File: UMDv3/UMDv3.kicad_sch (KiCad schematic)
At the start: 61 parts, among them CON101 USB-B1HSB6, CON104 JTAG-2X10-HDR, CON105 101-00405-75, CON106 UMDv3-CONN, CON107 HDR1X3, SW101 PTS645SM43SMTR92_LFS, SW102 PTS645SM43SMTR92_LFS, SW103 PTS645SM43SMTR92_LFS, SW104 PTS645SM43SMTR92_LFS, SW105 PTS645SM43SMTR92_LFS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

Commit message: betterer
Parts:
- removed U104: SSD1106-1.3-OLED-I2C, db-thparts:OLED-1.3-I2C, symbol db-sem:SSD1106-1.3-OLED-I2C
- added MEC105, MEC106: NSP-4-6-01, db-thparts:4-40-SCREW, symbol db-electromech:NSP-4-6-01
- added TP102: TP_2.25x3_ROUNDED, db-smt:TP_2.25x3_RND, symbol db-connectors:TP_2.25x3_ROUNDED
- added U104: SSD1106-0.96-OLED-I2C, db-thparts:OLED-0.96-I2C, symbol db-sem:SSD1106-0.96-OLED-I2C
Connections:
- net +3V3: now also U104.2 (VCC)
- net GND: now also TP102.1, U104.1 (GND)
- net SCL: now also U104.3 (SCL)
- net SDA: now also U104.4 (SDA)
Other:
- moved on the sheet: MEC101, MEC102, MEC103, MEC104, logo101

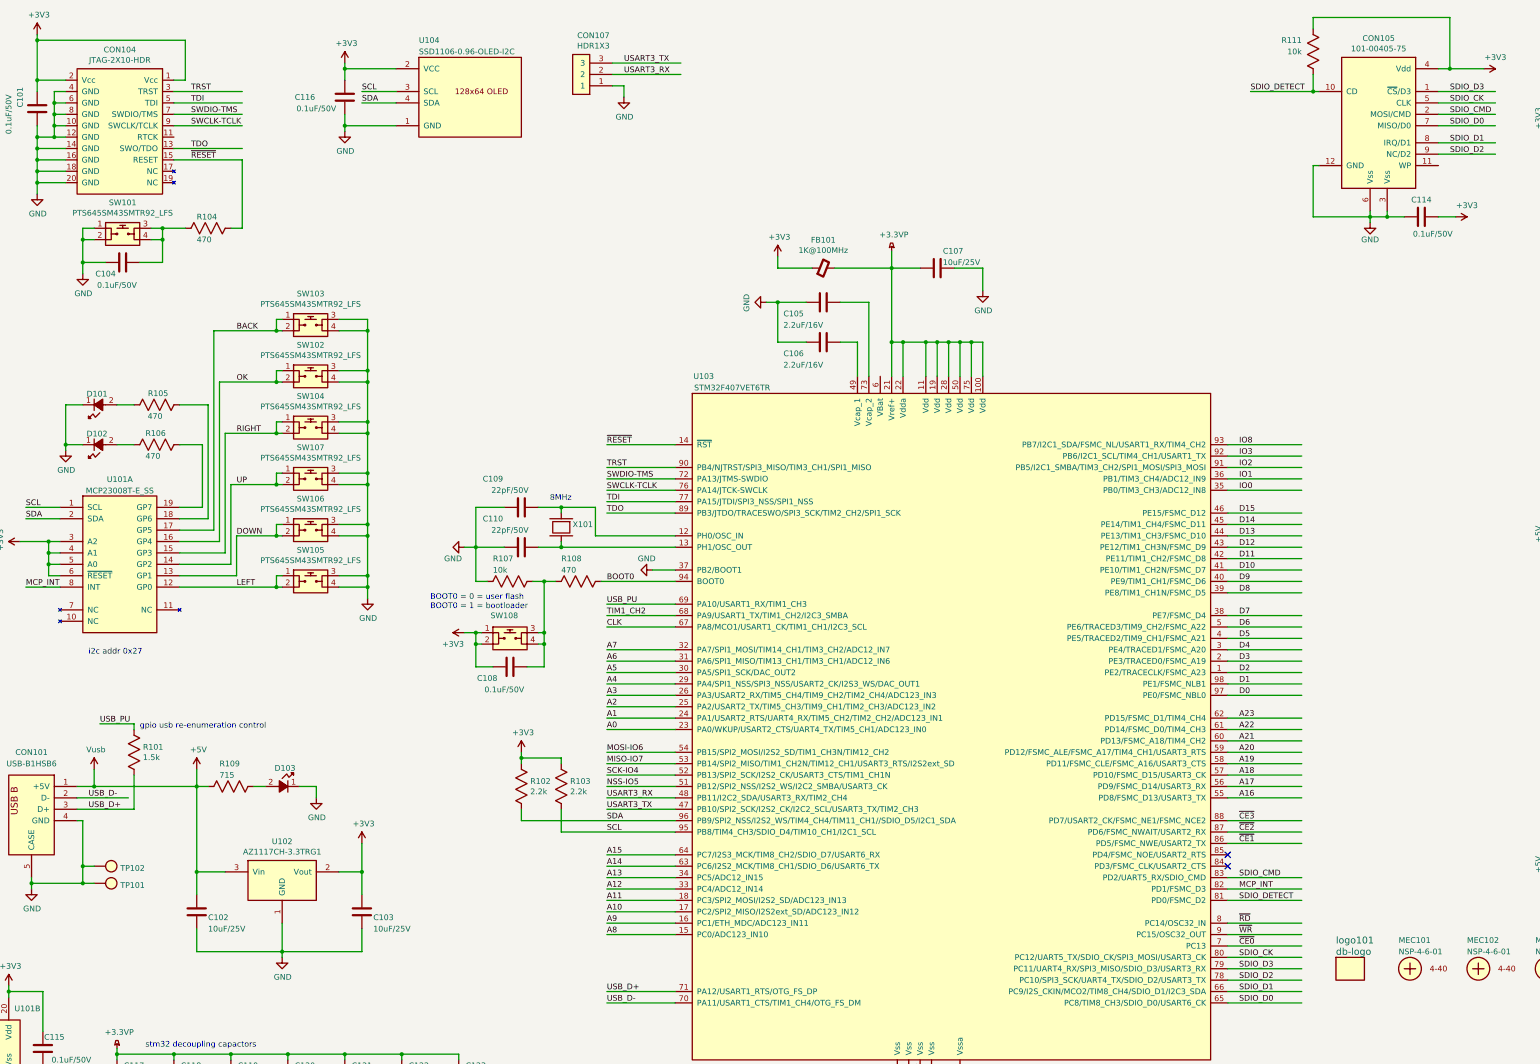
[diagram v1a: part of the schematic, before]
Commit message: more better decoupling capacitance
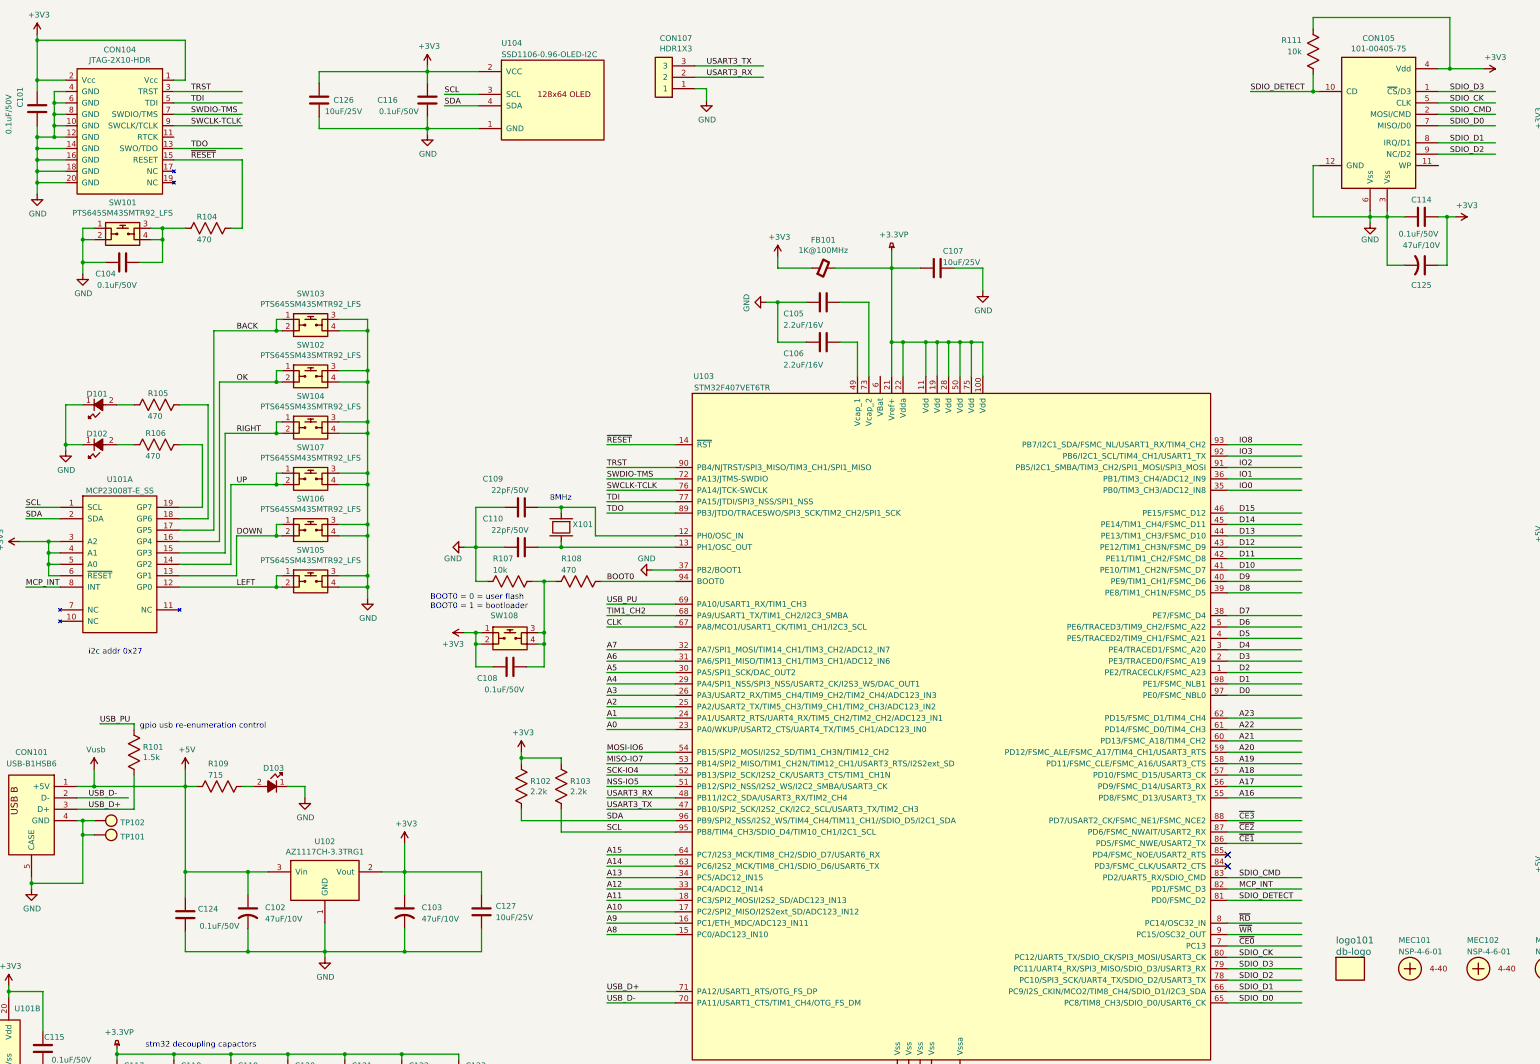
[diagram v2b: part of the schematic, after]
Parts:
- added C102, C103, C125: 47uF/10V, db-smt:1206_P, symbol db-passives:CP_1206
- added C124: 0.1uF/50V, db-smt:0603, symbol db-passives:C_0603
- renumbered C102 to C126, C103 to C127
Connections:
- net +3V3: now also C126.1, C103.1, C125.1
- net +5V: now also C102.1, C124.1; no longer C126.1
- net GND: now also C102.2, C103.2, C124.2, C125.2
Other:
- moved on the sheet: C116, C126, C127, CON107, D103, R109, TP101, TP102, U102, U104

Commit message: work
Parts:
- removed C125: 47uF/10V, db-smt:1206_P, symbol db-passives:CP_1206
- added C125: 10uF/25V, db-smt:0805, symbol db-passives:C_0805
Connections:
- net +3V3: now also C125.1
- net GND: now also C125.2
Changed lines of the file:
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@@
-    )
-  )
-  (symbol (lib_id "db-passives:CP_1206") (at 331.47 73.025 270) (unit 1)
-    (in_bom yes) (on_board yes) (dnp no)
-    (property "Reference" "C125" (at 331.47 77.47 90)
-      (effects (font (size 1.27 1.27)))
-    )
-    (property "Value" "47uF/10V" (at 331.47 68.58 90)
-      (effects (font (size 1.27 1.27)))
-    )
-    (property "Footprint" "db-smt:1206_P" (at 327.66 80.645 0)
-      (effects (font (size 0.762 0.762)) hide)
-    )
-    (property "Datasheet" "https://datasheets.kyocera-avx.com/TLJ.pdf" (at 332.74 76.327 0)
-      (effects (font (size 1.524 1.524)) hide)
-    )
-    (property "Digikey" "478-9009-1-ND" (at 335.28 78.867 0)
-      (effects (font (size 1.524 1.524)) hide)
-    )
-    (property "Description" "CAP TANT 47UF 20% 10V 1206" (at 337.82 78.74 0)
-      (effects (font (size 1.524 1.524)) hide)
-    )
-    (pin "1")
-    (pin "2")
-    (instances
-      (project "UMDv3"
-        (path "/fb4944d4-14cb-4442-bdd4-299490901fb8"
-          (reference "C125") (unit 1)
-        )
-      )
     )
   )
@@
         )
       )
+    )
+  )
+  (symbol (lib_id "db-passives:C_0805") (at 331.47 73.025 270) (unit 1)
+    (in_bom yes) (on_board yes) (dnp no)
+    (property "Reference" "C125" (at 329.565 69.215 90)
+      (effects (font (size 1.27 1.27)) (justify left))
+    )
+    (property "Value" "10uF/25V" (at 326.39 76.835 90)
+      (effects (font (size 1.27 1.27)) (justify left))
+    )
+    (property "Footprint" "db-smt:0805" (at 327.66 73.9902 0)
+      (effects (font (size 0.762 0.762)) hide)
+    )
+    (property "Datasheet" "" (at 334.01 73.66 0)
+      (effects (font (size 1.524 1.524)))
+    )
+    (property "Digikey" "1276-2891-1-ND" (at 336.55 76.2 0)
+      (effects (font (size 1.524 1.524)) hide)
+    )
+    (property "Description" "CAP CER 10UF 25V X5R 0805" (at 339.09 76.2 0)
+      (effects (font (size 1.524 1.524)) hide)
+    )
+    (pin "1")
+    (pin "2")
+    (instances
+      (project "UMDv3"
+        (path "/fb4944d4-14cb-4442-bdd4-299490901fb8"
+          (reference "C125") (unit 1)
+        )
+      )

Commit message: version 3.0.1 files
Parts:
- removed U104: SSD1106-0.96-OLED-I2C, db-thparts:OLED-0.96-I2C, symbol db-sem:SSD1106-0.96-OLED-I2C
- added U104: SSD1306-0.96-OLED-I2C, db-thparts:OLED-0.96-I2C, symbol db-sem:SSD1306-0.96-OLED-I2C
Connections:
- net +3V3: now also U104.2 (VCC)
- net GND: now also U104.1 (GND)
- net SCL: now also U104.3 (SCL)
- net SDA: now also U104.4 (SDA)
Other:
- moved on the sheet: C116, C126
